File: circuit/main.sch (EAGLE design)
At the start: 19 parts, among them IC2 LD398533RM, Q2 BSS138, Q3 12MHz, U1 ATTINY84-20SSU

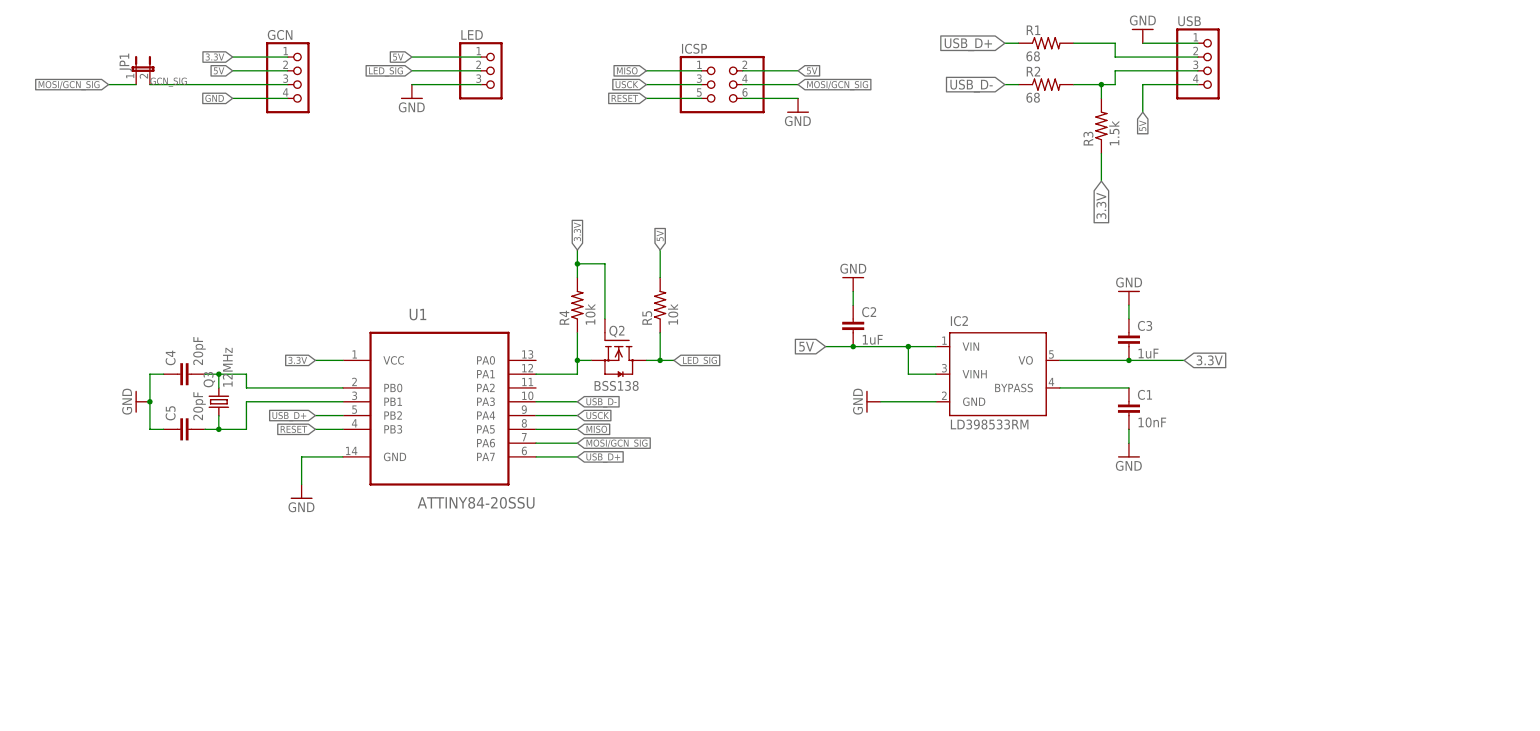
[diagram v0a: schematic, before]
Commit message: Updated v0.2 schematics to include title frame
Signed-off-by: Garrett Greenwood <garrettagreenwood@gmail.com>
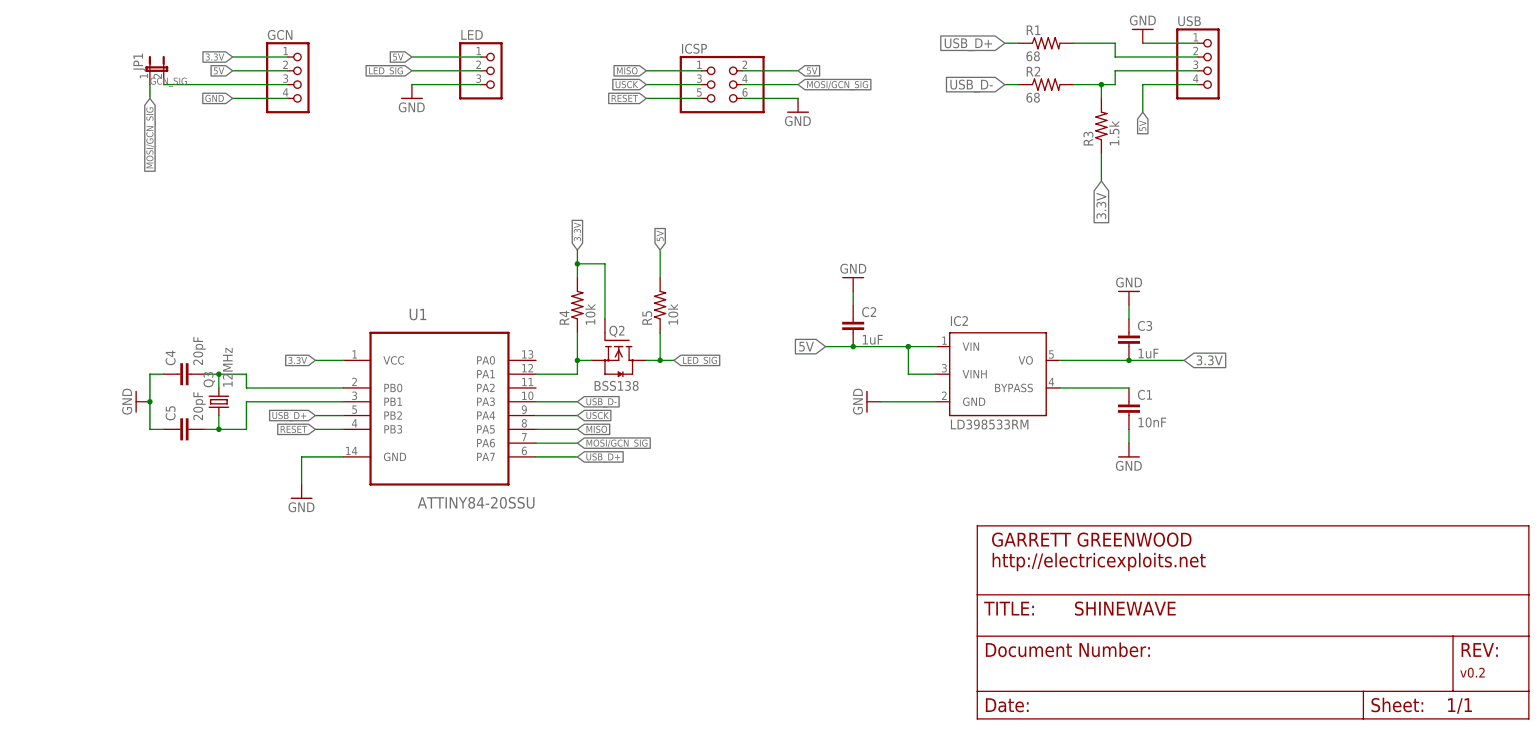
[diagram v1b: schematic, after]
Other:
- moved on the sheet: JP1
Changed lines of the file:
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@@
 <?xml version="1.0" encoding="utf-8"?>
 <!DOCTYPE eagle SYSTEM "eagle.dtd">
-<eagle version="7.4.0">
+<eagle version="7.5.0">
 <drawing>
 <settings>
@@
 <grid distance="0.1" unitdist="inch" unit="inch" style="lines" multiple="1" display="no" altdistance="0.01" altunitdist="inch" altunit="inch"/>
 <layers>
-<layer number="1" name="Top" color="4" fill="1" visible="yes" active="no"/>
-<layer number="16" name="Bottom" color="1" fill="1" visible="yes" active="no"/>
-<layer number="17" name="Pads" color="2" fill="1" visible="yes" active="no"/>
-<layer number="18" name="Vias" color="2" fill="1" visible="yes" active="no"/>
-<layer number="19" name="Unrouted" color="6" fill="1" visible="yes" active="no"/>
-<layer number="20" name="Dimension" color="15" fill="1" visible="yes" active="no"/>
-<layer number="21" name="tPlace" color="7" fill="1" visible="yes" active="no"/>
-<layer number="22" name="bPlace" color="7" fill="1" visible="yes" active="no"/>
-<layer number="23" name="tOrigins" color="15" fill="1" visible="yes" active="no"/>
-<layer number="24" name="bOrigins" color="15" fill="1" visible="yes" active="no"/>
-<layer number="25" name="tNames" color="7" fill="1" visible="yes" active="no"/>
-<layer number="26" name="bNames" color="7" fill="1" visible="yes" active="no"/>
-<layer number="27" name="tValues" color="7" fill="1" visible="yes" active="no"/>
-<layer number="28" name="bValues" color="7" fill="1" visible="yes" active="no"/>
+<layer number="1" name="Top" color="4" fill="1" visible="no" active="no"/>
+<layer number="16" name="Bottom" color="1" fill="1" visible="no" active="no"/>
+<layer number="17" name="Pads" color="2" fill="1" visible="no" active="no"/>
+<layer number="18" name="Vias" color="2" fill="1" visible="no" active="no"/>
+<layer number="19" name="Unrouted" color="6" fill="1" visible="no" active="no"/>
+<layer number="20" name="Dimension" color="15" fill="1" visible="no" active="no"/>
+<layer number="21" name="tPlace" color="7" fill="1" visible="no" active="no"/>
+<layer number="22" name="bPlace" color="7" fill="1" visible="no" active="no"/>
+<layer number="23" name="tOrigins" color="15" fill="1" visible="no" active="no"/>
+<layer number="24" name="bOrigins" color="15" fill="1" visible="no" active="no"/>
+<layer number="25" name="tNames" color="7" fill="1" visible="no" active="no"/>
+<layer number="26" name="bNames" color="7" fill="1" visible="no" active="no"/>
+<layer number="27" name="tValues" color="7" fill="1" visible="no" active="no"/>
+<layer number="28" name="bValues" color="7" fill="1" visible="no" active="no"/>
 <layer number="29" name="tStop" color="7" fill="3" visible="no" active="no"/>
 <layer number="30" name="bStop" color="7" fill="6" visible="no" active="no"/>
@@
 <layer number="35" name="tGlue" color="7" fill="4" visible="no" active="no"/>
 <layer number="36" name="bGlue" color="7" fill="5" visible="no" active="no"/>
-<layer number="37" name="tTest" color="7" fill="1" visible="yes" active="no"/>
-<layer number="38" name="bTest" color="7" fill="1" visible="yes" active="no"/>
+<layer number="37" name="tTest" color="7" fill="1" visible="no" active="no"/>
+<layer number="38" name="bTest" color="7" fill="1" visible="no" active="no"/>
 <layer number="39" name="tKeepout" color="4" fill="11" visible="no" active="no"/>
 <layer number="40" name="bKeepout" color="1" fill="11" visible="no" active="no"/>
@@
 <layer number="44" name="Drills" color="7" fill="1" visible="no" active="no"/>
 <layer number="45" name="Holes" color="7" fill="1" visible="no" active="no"/>
-<layer number="46" name="Milling" color="3" fill="1" visible="yes" active="no"/>
-<layer number="47" name="Measures" color="7" fill="1" visible="yes" active="no"/>
-<layer number="48" name="Document" color="7" fill="1" visible="yes" active="no"/>
-<layer number="49" name="Reference" color="7" fill="1" visible="yes" active="no"/>
-<layer number="51" name="tDocu" color="7" fill="1" visible="yes" active="no"/>
-<layer number="52" name="bDocu" color="7" fill="1" visible="yes" active="no"/>
+<layer number="46" name="Milling" color="3" fill="1" visible="no" active="no"/>
+<layer number="47" name="Measures" color="7" fill="1" visible="no" active="no"/>
+<layer number="48" name="Document" color="7" fill="1" visible="no" active="no"/>
+<layer number="49" name="Reference" color="7" fill="1" visible="no" active="no"/>
+<layer number="51" name="tDocu" color="7" fill="1" visible="no" active="no"/>
+<layer number="52" name="bDocu" color="7" fill="1" visible="no" active="no"/>
 <layer number="90" name="Modules" color="5" fill="1" visible="yes" active="yes"/>
 <layer number="91" name="Nets" color="2" fill="1" visible="yes" active="yes"/>
@@
 <part name="C1" library="resistor" deviceset="C-EU" device="C0603" value="10nF"/>
 <part name="GND9" library="supply1" deviceset="GND" device=""/>
+<part name="FRAME1" library="frames" deviceset="DINA4_L" device=""/>
 </parts>
 <sheets>
@@
 <instance part="R3" gate="G$1" x="185.42" y="109.22" rot="R90"/>
 <instance part="GND7" gate="1" x="7.62" y="58.42" rot="R270"/>
-<instance part="JP1" gate="A" x="7.62" y="119.38"/>
+<instance part="JP1" gate="A" x="10.16" y="119.38"/>
 <instance part="GND8" gate="1" x="129.54" y="111.76"/>
 <instance part="Q2" gate="G$1" x="96.52" y="68.58" smashed="yes" rot="R270">
@@
 <instance part="C1" gate="G$1" x="190.5" y="58.42"/>
 <instance part="GND9" gate="1" x="190.5" y="48.26"/>
+<instance part="FRAME1" gate="G$1" x="0" y="0"/>
+<instance part="FRAME1" gate="G$2" x="162.56" y="0"/>
 </instances>
 <busses>
@@
 <segment>
 <pinref part="GCN" gate="A" pin="3"/>
-<wire x1="35.56" y1="116.84" x2="10.16" y2="116.84" width="0.1524" layer="91"/>
+<wire x1="35.56" y1="116.84" x2="12.7" y2="116.84" width="0.1524" layer="91"/>
 <pinref part="JP1" gate="A" pin="2"/>
 <label x="10.16" y="116.84" size="1.27" layer="95"/>
@@
 <segment>
 <pinref part="JP1" gate="A" pin="1"/>
-<wire x1="7.62" y1="116.84" x2="2.54" y2="116.84" width="0.1524" layer="91"/>
-<label x="2.54" y="116.84" size="1.27" layer="95" rot="R180" xref="yes"/>
+<wire x1="10.16" y1="116.84" x2="10.16" y2="114.3" width="0.1524" layer="91"/>
+<label x="10.16" y="114.3" size="1.27" layer="95" rot="R270" xref="yes"/>
 </segment>
 </net>
@@
 </schematic>
 </drawing>
+<compatibility>
+<note version="6.3" minversion="6.2.2" severity="warning">
+Since Version 6.2.2 text objects can contain more than one line,
+which will not be processed correctly with this version.
+</note>
+</compatibility>
 </eagle>
